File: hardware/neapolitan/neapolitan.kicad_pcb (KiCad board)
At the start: 4 copper layers, 120 x 75 mm, 432 parts, among them J1 USB-MICRO-B, J10 GND_CLIP, J2 RF-SHIELD-FRAME, J3 RF-SHIELD-COVER, J4 MOUNTING_HOLE, J5 MOUNTING_HOLE, J6 MOUNTING_HOLE, J7 MOUNTING_HOLE, J8 MOUNTING_HOLE, J9 MOUNTING_HOLE, P1 1V8, P13 GPO1, P14 XCVR_CLKOUT, P15 INTR, P16 CLKIN, P17 GPO6, P18 OEB, P19 GPO3, P2 CLKOUT, P20 GPIO, P21 REF_IN, P22 I2S, P23 DBGEN, P24 TRST, P25 LPC_ISP, P26 LPC_JTAG, P27 MIXER_SDATA, P28 SD, P29 CPLD_JTAG, P3 GND, P30 BANK2_AUX, P31 MIXER_SCLK, P32 MIXER_ENX, P33 MIXER_RESETX, P34 MIX_BYPASS, P35 !MIX_BYPASS, P36 VAA, P37 SCL, P38 SDA, P39 SSP1_SCK, P4 ANTENNA, P40 SSP1_MOSI, P41 SSP1_MISO, P42 TX, P43 RX, P44 HP, P45 LP, P46 TX_MIX_BP, P47 RX_MIX_BP, P48 TX_AMP, P49 RX_AMP, P5 LEDS, P50 AMP_BYPASS, P51 !TX_AMP_PWR, P52 !RX_AMP_PWR, P53 CS_XCVR, P54 CS_AD, P55 TXENABLE, P56 RXENABLE, P57 XTAL2, P58 GCK1, P59 GCK2, P6 GPO4, P60 SGPIO_CLK, P61 DA0, P62 DA7, P63 DD0, P64 DD9, P65 DA4, P66 DD5, P67 RSSI, P68 SPIFI_CS, P69 VREGMODE, P7 GPO2, P70 EN_1V8, P71 ID, P72 GP_CLKIN, P73 P1_2, P74 P1_1, P75 GP_CLKIN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

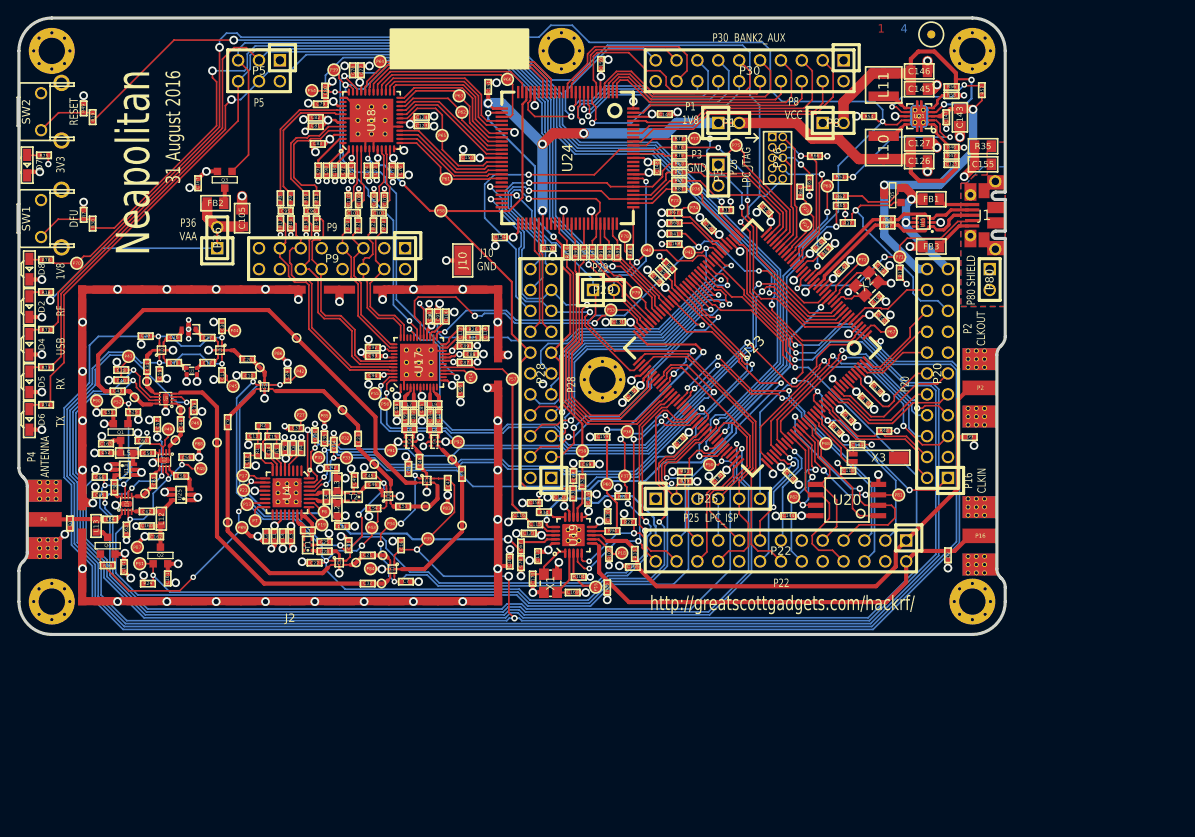
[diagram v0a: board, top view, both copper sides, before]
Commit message: Neapolitan: deleted MCU and other things not needed
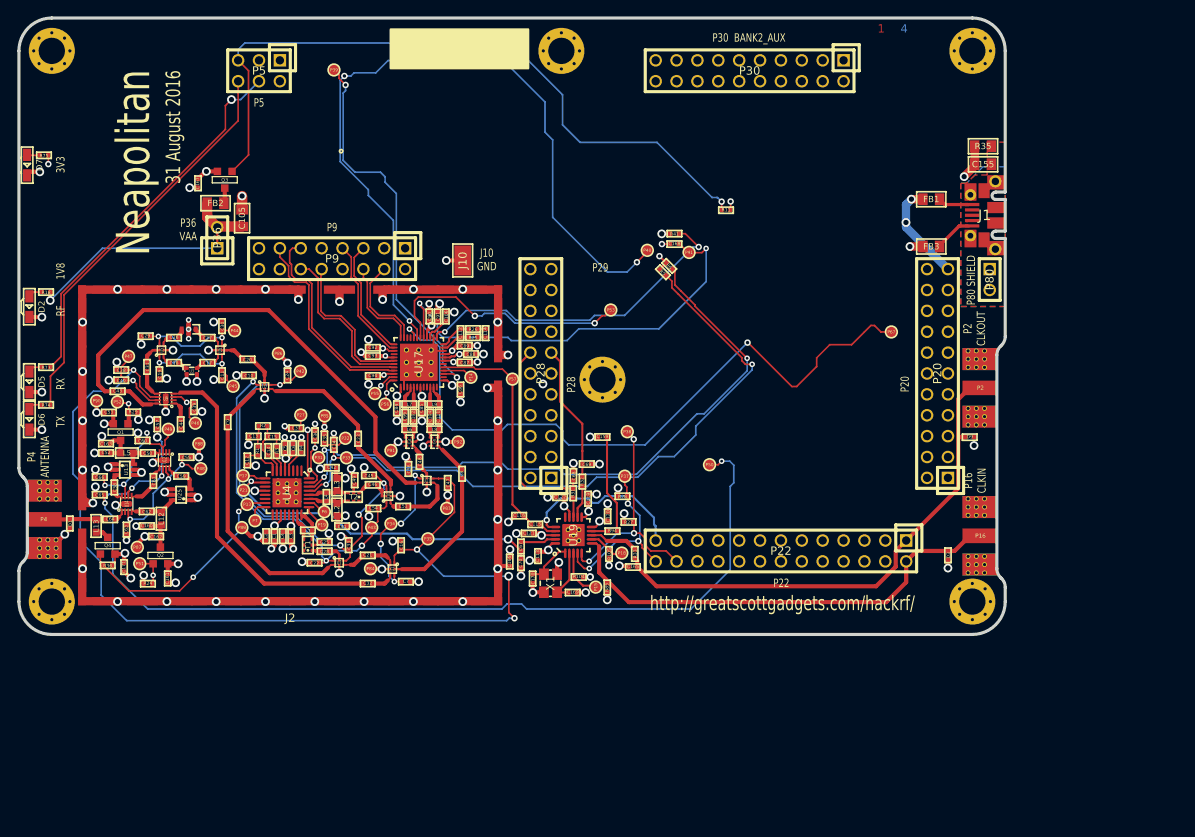
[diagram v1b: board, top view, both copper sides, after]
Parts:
- removed C100, C97, C98: 330nF, hackrf:GSG-0402
- removed C101, C103, C107, C108, C109, C110, C95, C96: 22pF, hackrf:GSG-0402
- removed C118, C157, C158, C164: 18pF, hackrf:GSG-0402
- removed C123, C128, C129, C130, C131, C132, C133, C134, C135, C136, C137, C138, C139, C140, C141, C142, C144, C147, C148, C149, C150, C151, C152, C153, C154, C71, C73, C75, C77, C79, C81, C83: 100nF, hackrf:GSG-0402
- removed C124, C72, C74, C76, C78, C80, C82: 2.2uF, hackrf:GSG-0402
- removed C125: 33pF, hackrf:GSG-0402
- removed C126, C127, C143, C145, C146: 10uF, hackrf:GSG-0805
- removed C156: 47pF, hackrf:GSG-0402
- removed D4: USBLED, gsg-modules:LTST-S220
- removed D8: 1V8LED, gsg-modules:LTST-S220
- removed L10, L11: 4u7, hackrf:GSG-NRG4026
- removed MARK1MM: VAL**, GSG-MARK1MM
- removed P1: 1V8, hackrf:GSG-HEADER-1x2
- removed P23: DBGEN, hackrf:GSG-TESTPOINT-50MIL
- removed P24: TRST, hackrf:GSG-TESTPOINT-50MIL
- removed P25: LPC_ISP, hackrf:GSG-HEADER-1x6
- removed P26: LPC_JTAG, hackrf:GSG-50MIL-HEADER-2x5-TH
- removed P29: CPLD_JTAG, hackrf:GSG-HEADER-1x2
- removed P3: GND, hackrf:GSG-HEADER-NOMARK-1x2
- removed P54: CS_AD, hackrf:GSG-TESTPOINT-50MIL
- removed P58: GCK1, hackrf:GSG-TESTPOINT-50MIL
- removed P59: GCK2, hackrf:GSG-TESTPOINT-50MIL
- removed P60: SGPIO_CLK, hackrf:GSG-TESTPOINT-50MIL
- removed P61: DA0, hackrf:GSG-TESTPOINT-50MIL
- removed P62: DA7, hackrf:GSG-TESTPOINT-50MIL
- removed P63: DD0, hackrf:GSG-TESTPOINT-50MIL
- removed P64: DD9, hackrf:GSG-TESTPOINT-50MIL
- removed P65: DA4, hackrf:GSG-TESTPOINT-50MIL
- removed P66: DD5, hackrf:GSG-TESTPOINT-50MIL
- removed P68: SPIFI_CS, hackrf:GSG-TESTPOINT-50MIL
- removed P69: VREGMODE, hackrf:GSG-TESTPOINT-50MIL
- removed P70: EN_1V8, hackrf:GSG-TESTPOINT-50MIL
- removed P71: ID, hackrf:GSG-TESTPOINT-50MIL
- removed P72, P75, P76, P77, P78, P79: GP_CLKIN, hackrf:GSG-TESTPOINT-50MIL
- removed P73: P1_2, hackrf:GSG-TESTPOINT-50MIL
- removed P74: P1_1, hackrf:GSG-TESTPOINT-50MIL
- removed P8: VCC, hackrf:GSG-HEADER-1x2
- removed P81: SPIFI_SIO2, hackrf:GSG-TESTPOINT-50MIL
- removed P82: SPIFI_SIO3, hackrf:GSG-TESTPOINT-50MIL
- removed Q5: MOSFET_P, gsg-modules:SOT23GDS
- removed R10, R13, R76, R8, R9: 1k, hackrf:GSG-0402
- removed R100, R19, R30, R34, R77, R78, R79, R80, R81, R86, R87, R88, R89, R90, R91, R96, R98, R99: 39, hackrf:GSG-0402
- removed R12, R37, R48, R49, R51, R52, R54, R59, R63, R64, R65, R66, R67, R68, R7, R93: 10k, hackrf:GSG-0402
- removed R14, R15, R16, R17: 4k7, hackrf:GSG-0402
- removed R20, R21, R22, R23, R57, R58, R62: 0, hackrf:GSG-0402
- removed R46, R55: 162k, hackrf:GSG-0402
- removed R47: 330k, hackrf:GSG-0402
- removed R56: 715k, hackrf:GSG-0402
- removed R69: 12k, hackrf:GSG-0402
- removed R72: 470, hackrf:GSG-0402
- removed SW1: DFU, hackrf:GSG-SWITCH-FSMRA
- removed SW2: RESET, hackrf:GSG-SWITCH-FSMRA
- removed TESTPOINT-30MIL-MASKONLY (x17): VAL**, GSG-TESTPOINT-30MIL-MASKONLY
- removed U15: LXES1TBCC2-004, hackrf:GSG-LXES1TBCC2-004
- removed U18: MAX5864, hackrf:GSG-QFN48-7
- removed U20: W25Q80BV, hackrf:GSG-SOIC8-208
- removed U21: TPS62410, hackrf:GSG-S-PVSON-N10
- removed U23: LPC4320FBD144, hackrf:GSG-LQFP144
- removed U24: GSG-XC2C64A-7VQG100C, hackrf:GSG-VQ100
- removed X2: MCU_XTAL, hackrf:GSG-XTAL3.2x2.5mm
- removed X3: RTC_XTAL, hackrf:GSG-XTAL-AB26TRQ
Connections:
- FB1 pad 2: /mcu/usb/power/VBUS -> (no net)
- J1 pad 2: Net-(J1-Pad2) -> (no net)
- J1 pad 3: Net-(J1-Pad3) -> (no net)
- J1 pad 4: Net-(J1-Pad4) -> (no net)
- P20 pad 1: /mcu/usb/power/VBAT -> (no net)
- P20 pad 10: /mcu/usb/power/GPIO3_13 -> (no net)
- P20 pad 11: /mcu/usb/power/GPIO3_14 -> (no net)
- P20 pad 12: /mcu/usb/power/GPIO3_15 -> (no net)
- P20 pad 14: /mcu/usb/power/ADC0_6 -> (no net)
- P20 pad 16: /mcu/usb/power/ADC0_2 -> (no net)
- P20 pad 17: /mcu/usb/power/VBUSCTRL -> (no net)
- P20 pad 18: /mcu/usb/power/ADC0_5 -> (no net)
- P20 pad 2: /mcu/usb/power/RTC_ALARM -> (no net)
- P20 pad 20: /mcu/usb/power/ADC0_0 -> (no net)
- P20 pad 21: /mcu/usb/power/VBUS -> (no net)
- P20 pad 22: /mcu/usb/power/VIN -> (no net)
- P20 pad 4: /mcu/usb/power/WAKEUP -> (no net)
- P20 pad 5: /mcu/usb/power/GPIO3_8 -> (no net)
- P20 pad 6: /mcu/usb/power/GPIO3_9 -> (no net)
- P20 pad 7: /mcu/usb/power/GPIO3_10 -> (no net)
- P20 pad 8: /mcu/usb/power/GPIO3_11 -> (no net)
- P20 pad 9: /mcu/usb/power/GPIO3_12 -> (no net)
- P22 pad 12: /mcu/usb/power/I2S0_RX_SCK -> (no net)
- P22 pad 13: /mcu/usb/power/I2S0_RX_SDA -> (no net)
- P22 pad 14: /mcu/usb/power/I2S0_RX_MCLK -> (no net)
- P22 pad 15: /mcu/usb/power/I2S0_RX_WS -> (no net)
- P22 pad 16: /mcu/usb/power/I2S0_TX_SCK -> (no net)
- P22 pad 17: /mcu/usb/power/I2S0_TX_MCLK -> (no net)
- P22 pad 19: /mcu/usb/power/U0_RXD -> (no net)
- P22 pad 20: /mcu/usb/power/U0_TXD -> (no net)
- P22 pad 21: /mcu/usb/power/P2_9 -> (no net)
- P22 pad 22: /mcu/usb/power/P2_13 -> (no net)
- P22 pad 23: /mcu/usb/power/P2_8 -> (no net)
- P22 pad 3: /mcu/usb/power/RESET -> (no net)
- P22 pad 5: /mcu/usb/power/I2C1_SCL -> (no net)
- P22 pad 6: /mcu/usb/power/I2C1_SDA -> (no net)
- P22 pad 7: /mcu/usb/power/SPIFI_MISO -> (no net)
- P22 pad 8: /mcu/usb/power/SPIFI_SCK -> (no net)
- P22 pad 9: /mcu/usb/power/SPIFI_MOSI -> (no net)
- P28 pad 10: /mcu/usb/power/SD_POW -> (no net)
- P28 pad 11: /mcu/usb/power/SD_CLK -> (no net)
- P28 pad 15: /mcu/usb/power/B1AUX14 -> (no net)
- P28 pad 16: /mcu/usb/power/B1AUX13 -> (no net)
- P28 pad 17: /mcu/usb/power/CPLD_TCK -> (no net)
- P28 pad 18: /mcu/usb/power/BANK2F3M2 -> (no net)
- P28 pad 19: /mcu/usb/power/CPLD_TDI -> (no net)
- P28 pad 20: /mcu/usb/power/BANK2F3M6 -> (no net)
- P28 pad 21: /mcu/usb/power/BANK2F3M12 -> (no net)
- P28 pad 22: /mcu/usb/power/BANK2F3M4 -> (no net)
- P28 pad 3: /mcu/usb/power/SD_CD -> (no net)
- P28 pad 4: /mcu/usb/power/SD_DAT3 -> (no net)
- P28 pad 5: /mcu/usb/power/SD_DAT2 -> (no net)
- P28 pad 6: /mcu/usb/power/SD_DAT1 -> (no net)
- P28 pad 7: /mcu/usb/power/SD_DAT0 -> (no net)
- P28 pad 8: /mcu/usb/power/SD_VOLT0 -> (no net)
- P28 pad 9: /mcu/usb/power/SD_CMD -> (no net)
- P30 pad 10: /mcu/usb/power/B2AUX9 -> (no net)
- P30 pad 11: /mcu/usb/power/B2AUX8 -> (no net)
- P30 pad 12: /mcu/usb/power/B2AUX7 -> (no net)
- P30 pad 13: /mcu/usb/power/B2AUX6 -> (no net)
- P30 pad 14: /mcu/usb/power/B2AUX5 -> (no net)
- P30 pad 15: /mcu/usb/power/B2AUX4 -> (no net)
- P30 pad 16: /mcu/usb/power/B2AUX3 -> (no net)
- P30 pad 17: /mcu/usb/power/B2AUX2 -> (no net)
- P30 pad 18: /mcu/usb/power/B2AUX1 -> (no net)
- P30 pad 19: /mcu/usb/power/GCK0 -> (no net)
- P30 pad 3: /mcu/usb/power/B2AUX16 -> (no net)
- P30 pad 4: /mcu/usb/power/B2AUX15 -> (no net)
- P30 pad 5: /mcu/usb/power/B2AUX14 -> (no net)
- P30 pad 6: /mcu/usb/power/B2AUX13 -> (no net)
- P30 pad 7: /mcu/usb/power/B2AUX12 -> (no net)
- P30 pad 8: /mcu/usb/power/B2AUX11 -> (no net)
- P30 pad 9: /mcu/usb/power/B2AUX10 -> (no net)
- P5 pad 3: /mcu/usb/power/LED1 -> (no net)
- U12 pad 2: Net-(U12-Pad2) -> (no net)
- U14 pad 2: Net-(U14-Pad2) -> (no net)
- U17 pad 12: Net-(U17-Pad12) -> (no net)
- U17 pad 14: Net-(U17-Pad14) -> (no net)
- U17 pad 18: Net-(U17-Pad18) -> (no net)
- U17 pad 3: Net-(U17-Pad3) -> (no net)
- U17 pad 33: Net-(U17-Pad33) -> (no net)
- U17 pad 34: Net-(U17-Pad34) -> (no net)
- U17 pad 40: Net-(U17-Pad40) -> (no net)
- U17 pad 6: Net-(U17-Pad6) -> (no net)
- U17 pad 8: Net-(U17-Pad8) -> (no net)
- U17 pad 9: Net-(U17-Pad9) -> (no net)
- U19 pad 15: MCU_CLK -> (no net)
- U4 pad 1: Net-(U4-Pad1) -> (no net)
- U4 pad 11: Net-(U4-Pad11) -> (no net)
- U4 pad 13: Net-(U4-Pad13) -> (no net)
- U4 pad 14: Net-(U4-Pad14) -> (no net)
- U4 pad 17: Net-(U4-Pad17) -> (no net)
- U4 pad 18: Net-(U4-Pad18) -> (no net)
- U4 pad 2: Net-(U4-Pad2) -> (no net)
- U4 pad 20: Net-(U4-Pad20) -> (no net)
- U4 pad 21: Net-(U4-Pad21) -> (no net)
- U4 pad 3: Net-(U4-Pad3) -> (no net)
- U9 pad 2: Net-(U9-Pad2) -> (no net)
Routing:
- net LP: track 225.5 -> 14.8 mm, vias 3 -> 2
- net TX_MIX_BP: track 215.0 -> 5.87 mm, vias 2 -> 1
- net GND: track 592.3 -> 401.6 mm, vias 230 -> 141
- net HP: track 202.5 -> 14.2 mm, vias 3 -> 2
- net RX_MIX_BP: track 192.3 -> 8.74 mm, vias 2 -> 1
- net /mcu/usb/power/RESET: track 182.8 -> 0.00 mm, vias 4 -> 0
- net /mcu/usb/power/EN1V8: track 180.4 -> 0.00 mm, vias 3 -> 0
- net /mcu/usb/power/P2_8: track 154.4 -> 0.00 mm, vias 3 -> 0
- net /mcu/usb/power/LED1: track 141.5 -> 0.00 mm, vias 1 -> 0
- net !RX_AMP_PWR: track 130.1 -> 3.94 mm, vias 2 -> 1
- net TX_AMP: track 143.2 -> 17.2 mm, vias 4 -> 3
- net /mcu/usb/power/LED3: track 161.0 -> 48.8 mm, vias 1 -> 0
- net !MIX_BYPASS: track 237.4 -> 125.7 mm, vias 5 -> 4
- net RX_AMP: track 130.3 -> 18.8 mm, vias 4 -> 3
- net /mcu/usb/power/LED2: track 136.7 -> 46.0 mm, vias 2 -> 1
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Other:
- board text removed: "P1 1V8"
- board text removed: "P25 LPC_ISP"
- board text removed: "P26 LPC_JTAG"
- board text removed: "P3 GND"
- board text removed: "P8 VCC"

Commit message: Neapolitan: deleted end plate drawings
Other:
- board text removed: "ANTENNA"
- board text removed: "CLKIN"
- board text removed: "CLKOUT"
- board text removed: "DFU"
- board text removed: "LED1"
- board text removed: "RESET"
- board text removed: "USB"
- board text removed: "end plate templates for optional Hammond 1455J1201 enclosure"
- board text removed: "front end plate"
- board text removed: "rear end plate"
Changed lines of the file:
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@@
     (links 692)
     (no_connects 2)
-    (area 59.329499 99.809499 180.670501 175.190501)
+    (area 57.669958 17.0375 275.101601 176.1916)
     (thickness 1.6002)
-    (drawings 165)
+    (drawings 75)
     (tracks 1821)
     (zones 0)
@@
   (gr_line (start 178.85 122.075) (end 180 122.075) (angle 90) (layer Edge.Cuts) (width 0.381))
   (gr_line (start 180 121.175) (end 178.85 121.175) (angle 90) (layer Edge.Cuts) (width 0.381))
-  (gr_line (start 262.245 35) (end 262.245 43) (angle 90) (layer Cmts.User) (width 0.2032))
-  (gr_line (start 256.755 35) (end 256.755 43) (angle 90) (layer Cmts.User) (width 0.2032))
-  (gr_line (start 231.245 71) (end 231.245 79) (angle 90) (layer Cmts.User) (width 0.2032))
-  (gr_line (start 225.755 71) (end 225.755 79) (angle 90) (layer Cmts.User) (width 0.2032))
-  (gr_line (start 207.755 79) (end 207.755 71) (angle 90) (layer Cmts.User) (width 0.2032))
-  (gr_line (start 213.245 71) (end 213.245 79) (angle 90) (layer Cmts.User) (width 0.2032))
   (gr_line (start 60.58 155.94) (end 60.44 155.8) (angle 90) (layer Edge.Cuts) (width 0.381))
   (gr_line (start 60.44 166.2) (end 60.58 166.06) (angle 90) (layer Edge.Cuts) (width 0.381))
@@
   (gr_line (start 61.02 157) (end 61.02 165) (angle 90) (layer Edge.Cuts) (width 0.381))
   (gr_line (start 178.98 141) (end 178.98 167) (angle 90) (layer Edge.Cuts) (width 0.381))
-  (gr_line (start 246.5 72.275) (end 252.5 72.275) (angle 90) (layer Cmts.User) (width 0.2032))
-  (gr_line (start 246.5 76.275) (end 252.5 76.275) (angle 90) (layer Cmts.User) (width 0.2032))
-  (gr_line (start 198.5 38) (end 198.5 42.5) (angle 90) (layer Cmts.User) (width 0.2032))
-  (gr_line (start 198.5 74) (end 198.5 78.5) (angle 90) (layer Cmts.User) (width 0.2032))
-  (gr_text USB (at 249.5 84) (layer Cmts.User)
-    (effects (font (size 1.5 1) (thickness 0.2)))
-  )
-  (gr_text CLKOUT (at 228.5 84) (layer Cmts.User)
-    (effects (font (size 1.5 1) (thickness 0.2)))
-  )
-  (gr_text CLKIN (at 210.5 84) (layer Cmts.User)
-    (effects (font (size 1.5 1) (thickness 0.2)))
-  )
-  (gr_line (start 243.5 74.275) (end 255.5 74.275) (angle 90) (layer Cmts.User) (width 0.2032))
-  (gr_line (start 246.5 70.775) (end 246.5 77.775) (angle 90) (layer Cmts.User) (width 0.2032))
-  (gr_line (start 252.5 70.775) (end 252.5 77.775) (angle 90) (layer Cmts.User) (width 0.2032))
-  (gr_circle (center 249.5 74.275) (end 251.5 74.275) (layer Cmts.User) (width 0.2032))
-  (gr_circle (center 252.5 74.275) (end 250.5 74.275) (layer Cmts.User) (width 0.2032))
-  (gr_circle (center 246.5 74.275) (end 248.5 74.275) (layer Cmts.User) (width 0.2032))
-  (gr_line (start 249.5 68) (end 249.5 81) (angle 90) (layer Cmts.User) (width 0.2032))
-  (gr_line (start 228.5 68) (end 228.5 81) (angle 90) (layer Cmts.User) (width 0.2032))
-  (gr_line (start 210.5 68) (end 210.5 81) (angle 90) (layer Cmts.User) (width 0.2032))
-  (gr_circle (center 228.5 74.86) (end 231.75 74.86) (layer Cmts.User) (width 0.2032))
-  (gr_circle (center 210.5 74.86) (end 213.75 74.86) (layer Cmts.User) (width 0.2032))
-  (gr_line (start 205 74.86) (end 234 74.86) (angle 90) (layer Cmts.User) (width 0.2032))
-  (gr_line (start 275 65) (end 275 84) (angle 90) (layer Cmts.User) (width 0.2032))
-  (gr_line (start 271 88) (end 201 88) (angle 90) (layer Cmts.User) (width 0.2032))
-  (gr_line (start 197 84) (end 197 65) (angle 90) (layer Cmts.User) (width 0.2032))
-  (gr_line (start 201 61) (end 271 61) (angle 90) (layer Cmts.User) (width 0.2032))
-  (gr_arc (start 271 65) (end 271 61) (angle 90) (layer Cmts.User) (width 0.2032))
-  (gr_arc (start 271 84) (end 275 84) (angle 90) (layer Cmts.User) (width 0.2032))
-  (gr_arc (start 201 84) (end 201 88) (angle 90) (layer Cmts.User) (width 0.2032))
-  (gr_arc (start 201 65) (end 197 65) (angle 90) (layer Cmts.User) (width 0.2032))
-  (gr_circle (center 271 65) (end 274 65) (layer Cmts.User) (width 0.2032))
-  (gr_circle (center 271 84) (end 274 84) (layer Cmts.User) (width 0.2032))
-  (gr_circle (center 201 84) (end 201 87) (layer Cmts.User) (width 0.2032))
-  (gr_circle (center 201 65) (end 198 65) (layer Cmts.User) (width 0.2032))
-  (gr_line (start 198 77.31) (end 204 77.31) (angle 90) (layer Cmts.User) (width 0.2032))
-  (gr_line (start 198 75.31) (end 204 75.31) (angle 90) (layer Cmts.User) (width 0.2032))
-  (gr_line (start 199 75.51) (end 205 75.51) (angle 90) (layer Cmts.User) (width 0.2032))
-  (gr_line (start 199 77.11) (end 205 77.11) (angle 90) (layer Cmts.User) (width 0.2032))
-  (gr_text ANTENNA (at 259.5 48) (layer Cmts.User)
-    (effects (font (size 1.5 1) (thickness 0.2)))
-  )
-  (gr_text TX (at 247.338 48) (layer Cmts.User)
-    (effects (font (size 1.5 1) (thickness 0.2)))
-  )
-  (gr_text RX (at 242.766 48) (layer Cmts.User)
-    (effects (font (size 1.5 1) (thickness 0.2)))
-  )
-  (gr_text LED1 (at 238.194 48) (layer Cmts.User)
-    (effects (font (size 1.5 1) (thickness 0.2)))
-  )
-  (gr_text RF (at 233.622 48) (layer Cmts.User)
-    (effects (font (size 1.5 1) (thickness 0.2)))
-  )
-  (gr_text 1V8 (at 229.05 48) (layer Cmts.User)
-    (effects (font (size 1.5 1) (thickness 0.2)))
-  )
-  (gr_text 3V3 (at 216.4 48) (layer Cmts.User)
-    (effects (font (size 1.5 1) (thickness 0.2)))
-  )
-  (gr_text DFU (at 222.9 48) (layer Cmts.User)
-    (effects (font (size 1.5 1) (thickness 0.2)))
-  )
-  (gr_text RESET (at 209.9 48) (layer Cmts.User)
-    (effects (font (size 1.5 1) (thickness 0.2)))
-  )
-  (gr_circle (center 247.338 39.21) (end 248.338 39.21) (layer Cmts.User) (width 0.2032))
-  (gr_circle (center 242.766 39.21) (end 243.766 39.21) (layer Cmts.User) (width 0.2032))
-  (gr_circle (center 238.194 39.21) (end 239.194 39.21) (layer Cmts.User) (width 0.2032))
-  (gr_circle (center 233.622 39.21) (end 234.622 39.21) (layer Cmts.User) (width 0.2032))
-  (gr_circle (center 229.05 39.21) (end 230.05 39.21) (layer Cmts.User) (width 0.2032))
-  (gr_circle (center 216.4 39.21) (end 217.4 39.21) (layer Cmts.User) (width 0.2032))
-  (gr_line (start 213 39.21) (end 250 39.21) (angle 90) (layer Cmts.User) (width 0.2032))
-  (gr_circle (center 222.9 35.5) (end 224.9 35.5) (layer Cmts.User) (width 0.2032))
-  (gr_circle (center 209.9 35.5) (end 211.9 35.5) (layer Cmts.User) (width 0.2032))
-  (gr_line (start 205.5 35.5) (end 226.5 35.5) (angle 90) (layer Cmts.User) (width 0.2032))
-  (gr_circle (center 259.5 38.86) (end 262.75 38.86) (layer Cmts.User) (width 0.2032))
-  (gr_line (start 256 38.86) (end 263 38.86) (angle 90) (layer Cmts.User) (width 0.2032))
-  (gr_line (start 199 41.11) (end 205 41.11) (angle 90) (layer Cmts.User) (width 0.2032))
-  (gr_line (start 199 39.51) (end 205 39.51) (angle 90) (layer Cmts.User) (width 0.2032))
-  (gr_line (start 198 39.31) (end 204 39.31) (angle 90) (layer Cmts.User) (width 0.2032))
-  (gr_line (start 198 41.31) (end 204 41.31) (angle 90) (layer Cmts.User) (width 0.2032))
-  (gr_line (start 247.338 43) (end 247.338 34) (angle 90) (layer Cmts.User) (width 0.2032))
-  (gr_line (start 242.766 43) (end 242.766 34) (angle 90) (layer Cmts.User) (width 0.2032))
-  (gr_line (start 238.194 43) (end 238.194 34) (angle 90) (layer Cmts.User) (width 0.2032))
-  (gr_line (start 233.622 43) (end 233.622 34) (angle 90) (layer Cmts.User) (width 0.2032))
-  (gr_line (start 229.05 43) (end 229.05 34) (angle 90) (layer Cmts.User) (width 0.2032))
-  (gr_line (start 216.4 43) (end 216.4 34) (angle 90) (layer Cmts.User) (width 0.2032))
-  (gr_line (start 222.9 43) (end 222.9 32) (angle 90) (layer Cmts.User) (width 0.2032))
-  (gr_line (start 209.9 43) (end 209.9 32) (angle 90) (layer Cmts.User) (width 0.2032))
-  (gr_line (start 259.5 43) (end 259.5 32) (angle 90) (layer Cmts.User) (width 0.2032))
-  (gr_text "rear end plate" (at 236 91) (layer Cmts.User)
-    (effects (font (size 2 1.5) (thickness 0.375)))
-  )
-  (gr_text "front end plate" (at 236 55) (layer Cmts.User)
-    (effects (font (size 2 1.5) (thickness 0.375)))
-  )
-  (gr_text "end plate templates for optional Hammond 1455J1201 enclosure" (at 236 19) (layer Cmts.User)
-    (effects (font (size 2 1.5) (thickness 0.375)))
-  )
-  (gr_circle (center 201 29) (end 198 29) (layer Cmts.User) (width 0.2032))
-  (gr_circle (center 201 48) (end 201 51) (layer Cmts.User) (width 0.2032))
-  (gr_circle (center 271 48) (end 274 48) (layer Cmts.User) (width 0.2032))
-  (gr_circle (center 271 29) (end 274 29) (layer Cmts.User) (width 0.2032))
-  (gr_arc (start 201 29) (end 197 29) (angle 90) (layer Cmts.User) (width 0.2032))
-  (gr_arc (start 201 48) (end 201 52) (angle 90) (layer Cmts.User) (width 0.2032))
-  (gr_arc (start 271 48) (end 275 48) (angle 90) (layer Cmts.User) (width 0.2032))
-  (gr_arc (start 271 29) (end 271 25) (angle 90) (layer Cmts.User) (width 0.2032))
-  (gr_line (start 201 25) (end 271 25) (angle 90) (layer Cmts.User) (width 0.2032))
-  (gr_line (start 197 48) (end 197 29) (angle 90) (layer Cmts.User) (width 0.2032))
-  (gr_line (start 271 52) (end 201 52) (angle 90) (layer Cmts.User) (width 0.2032))
-  (gr_line (start 275 29) (end 275 48) (angle 90) (layer Cmts.User) (width 0.2032))
   (gr_circle (center 125.2 165.2) (end 125.4 165.2) (layer F.SilkS) (width 0.2032))
   (gr_circle (center 95.4 155) (end 95.6 155) (layer F.SilkS) (width 0.2032))

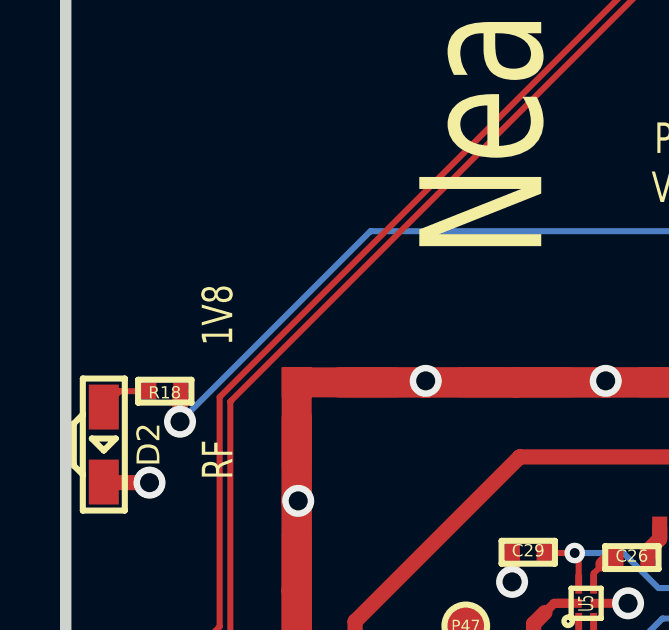
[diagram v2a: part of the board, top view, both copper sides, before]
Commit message: Neapolitan: barrel jack and USB power sources that override USB power on main board
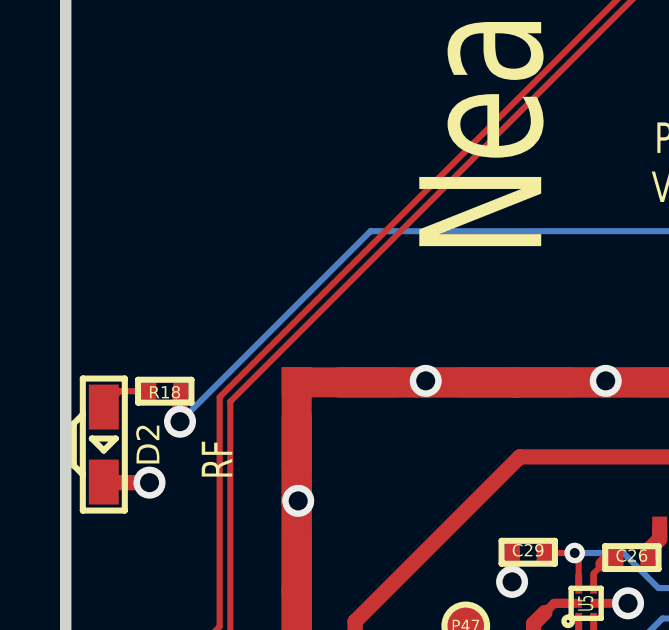
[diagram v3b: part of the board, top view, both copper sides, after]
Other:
- board text removed: "1V8"
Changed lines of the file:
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@@
     (area 57.669958 17.0375 275.101601 176.1916)
     (thickness 1.6002)
-    (drawings 75)
+    (drawings 74)
     (tracks 1821)
     (zones 0)
@@
   (gr_arc (start 64 171) (end 64 175) (angle 90) (layer Edge.Cuts) (width 0.381))
   (gr_arc (start 64 104) (end 60 104) (angle 90) (layer Edge.Cuts) (width 0.381))
-  (gr_text 1V8 (at 65.08 130.804 90) (layer F.SilkS)
-    (effects (font (size 1.016 0.762) (thickness 0.1905)))
-  )
   (gr_text 3V3 (at 65.08 117.85 90) (layer F.SilkS)
     (effects (font (size 1.016 0.762) (thickness 0.1905)))
